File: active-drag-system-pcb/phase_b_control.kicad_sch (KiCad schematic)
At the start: 18 parts, among them Q1 SIR182DP-T1-RE3, Q2 SIR182DP-T1-RE3, U11 IR2103, U12 INA180A3

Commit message: Add other two phases; remove CYW43 for scope reasons
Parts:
- renumbered C30 to C36, C31 to C37, C32 to C38, C33 to C39, C34 to C40, C35 to C41, D1 to D3, D2 to D4, Q1 to Q3, Q2 to Q4, R11 to R16, R10 to R17, R12 to R18, R13 to R19, R14 to R20, R15 to R21, U11 to U13, U12 to U14
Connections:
- net CURRENT_SENSE_A renamed CURRENT_SENSE_B
- net PHASE_A renamed PHASE_B
- net VOLTAGE_SENSE_A renamed VOLTAGE_SENSE_B

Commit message: Swapped out regulators for higher current output; removed 8.4 V regulator; now two grounds (power and analog)
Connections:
- net +8V renamed +BATT
- net GND renamed GNDA
- net GNDA: no longer C38.2, R18.2, U14.4 (-)
- new net GNDPWR: C38.2, R18.2, U14.4 (-)

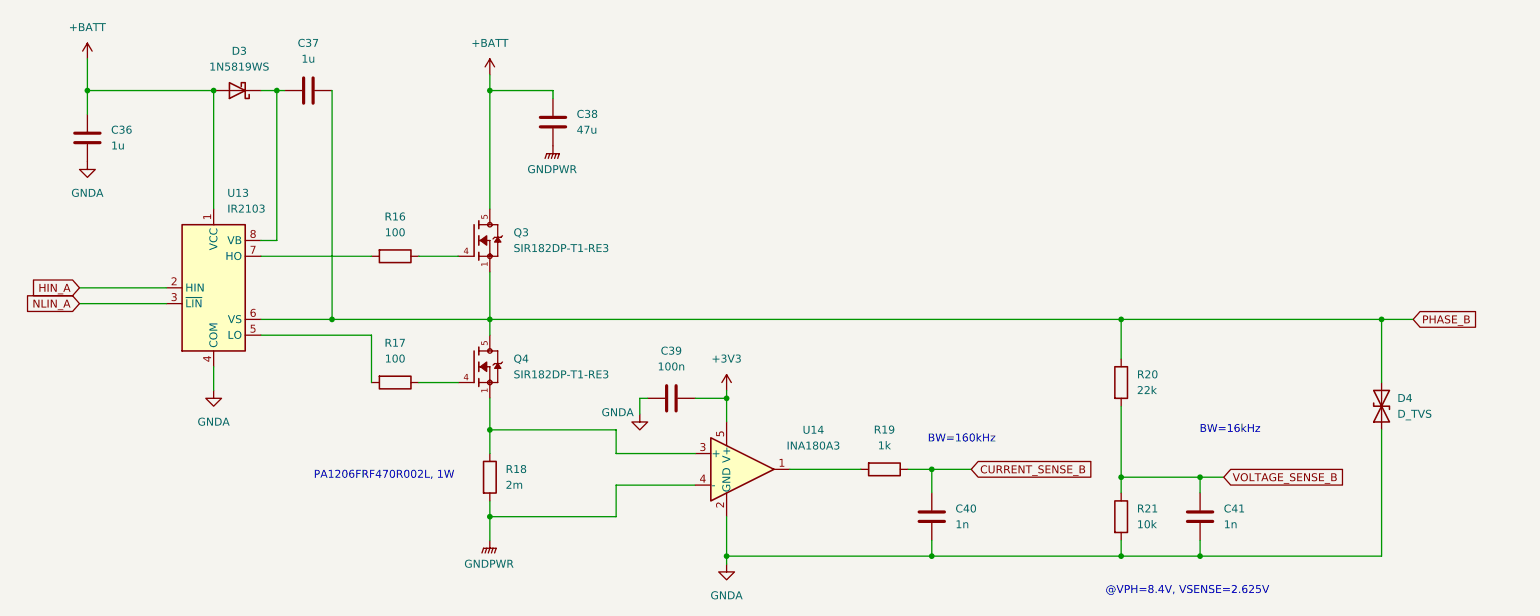
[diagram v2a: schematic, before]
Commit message: Literally everything has footprints and is pretty connected together on schematic except for IIM
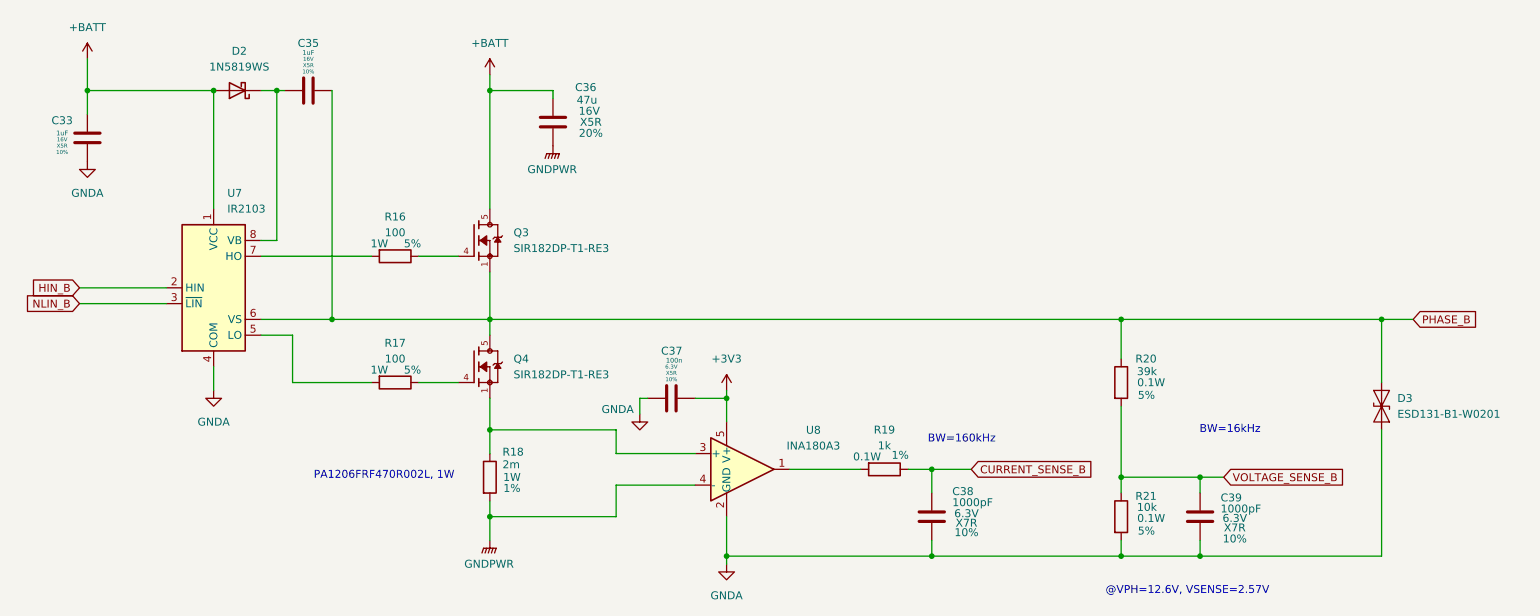
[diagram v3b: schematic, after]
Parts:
- removed C36: 1u, symbol Device:C
- removed C41: 1n, symbol Device:C
- removed D4: D_TVS, symbol Device:D_TVS
- added C33: 1uF, Capacitor_SMD:C_0402_1005Metric_Pad0.74x0.62mm_HandSolder, symbol Device:C
- added C37: 100n, Capacitor_SMD:C_0201_0603Metric_Pad0.64x0.40mm_HandSolder, symbol Device:C
- added D3: ESD131-B1-W0201, Diode_SMD:Infineon_SG-WLL-2-3_0.58x0.28_P0.36mm, symbol Diode:ESD131-B1-W0201
- C35: renamed from C37; value 1u -> 1uF; footprint (none) -> Capacitor_SMD:C_0402_1005Metric_Pad0.74x0.62mm_HandSolder; Dielectric (none) -> X5R; Max Voltage (none) -> 16V; Tolerance (none) -> 10%
- C36: renamed from C38; footprint (none) -> Capacitor_SMD:C_1210_3225Metric_Pad1.33x2.70mm_HandSolder; Dielectric (none) -> X5R; Max Voltage (none) -> 16V; Tolerance (none) -> 20%
- C38: renamed from C40; value 1n -> 1000pF; footprint (none) -> Capacitor_SMD:C_0402_1005Metric_Pad0.74x0.62mm_HandSolder; Dielectric (none) -> X7R; Max Voltage (none) -> 6.3V; Tolerance (none) -> 10%
- C39: value 100n -> 1000pF; footprint (none) -> Capacitor_SMD:C_0402_1005Metric_Pad0.74x0.62mm_HandSolder; Dielectric (none) -> X7R; Max Voltage (none) -> 6.3V; Tolerance (none) -> 10%
- R16, R17: footprint (none) -> Resistor_SMD:R_2512_6332Metric_Pad1.40x3.35mm_HandSolder; Power (none) -> 1W; Tolerance (none) -> 5%
- R18: footprint (none) -> Resistor_SMD:R_1206_3216Metric_Pad1.30x1.75mm_HandSolder; Power (none) -> 1W; Tolerance (none) -> 1%
- R19: footprint (none) -> Resistor_SMD:R_0402_1005Metric_Pad0.72x0.64mm_HandSolder; Power (none) -> 0.1W; Tolerance (none) -> 1%
- R20: value 22k -> 39k; footprint (none) -> Resistor_SMD:R_0402_1005Metric_Pad0.72x0.64mm_HandSolder; Power (none) -> 0.1W; Tolerance (none) -> 5%
- R21: footprint (none) -> Resistor_SMD:R_0402_1005Metric_Pad0.72x0.64mm_HandSolder; Power (none) -> 0.1W; Tolerance (none) -> 5%
- renumbered D3 to D2, U13 to U7, U14 to U8
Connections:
- net +3V3: now also C37.2; no longer C39.1
- net +BATT: now also C33.1
- net GNDA: now also C33.2, C37.1, D3.1 (A1)
- net PHASE_B: now also D3.2 (A2)
- net VOLTAGE_SENSE_B: now also C39.1
- net HIN_A renamed HIN_B
- net NLIN_A renamed NLIN_B
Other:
- note added: "@VPH=12.6V, VSENSE=2.57V"
- note removed: "@VPH=8.4V, VSENSE=2.625V"

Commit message: Updated Footprint library; Started component placement for 5V regulator
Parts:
- Q3, Q4: footprint SIR182DP-T1-RE3:TRANS_SIR182DP-T1-RE3 -> ADS_Library:TRANS_SIR182DP-T1-RE3
- U7: value IR2103 -> IR2103STRPBF; footprint (none) -> ADS_Library:SO8N_INF-L
